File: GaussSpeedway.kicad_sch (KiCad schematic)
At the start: 47 parts

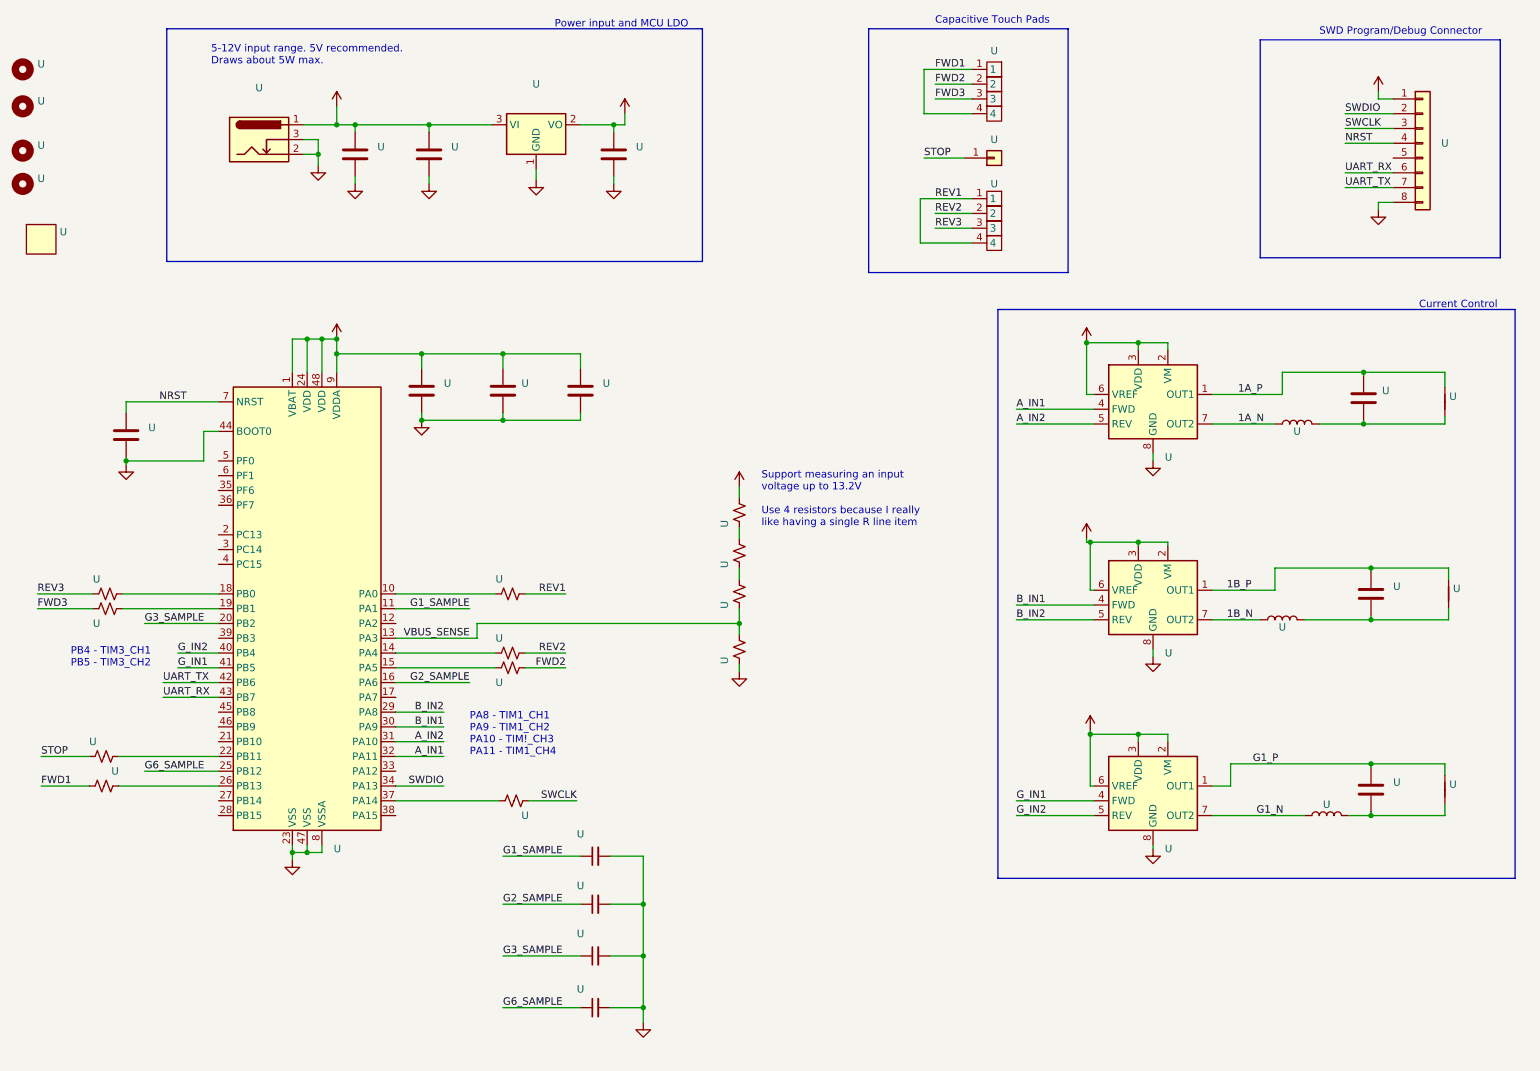
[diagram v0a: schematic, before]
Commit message: Revert an accidental eeschema nightly infection
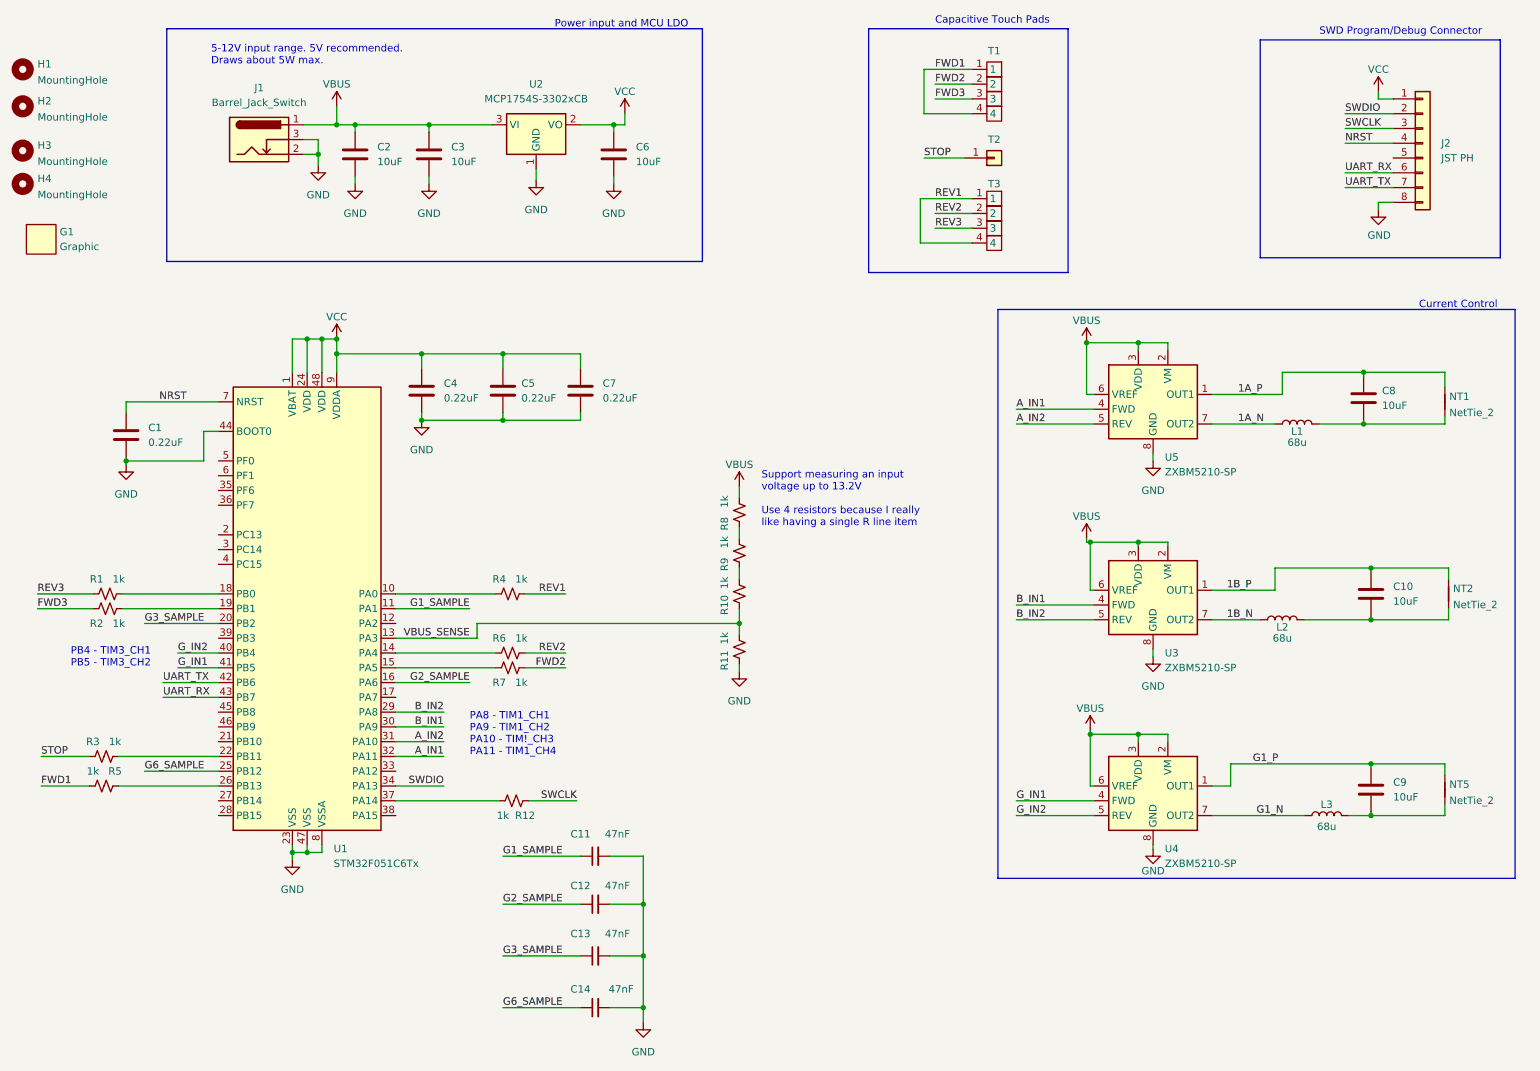
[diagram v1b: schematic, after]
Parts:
- C1, C4, C5, C7: renamed from U; value (none) -> 0.22uF; footprint (none) -> Capacitor_SMD:C_0603_1608Metric
- C10, C2, C3, C6, C8, C9: renamed from U; value (none) -> 10uF; footprint (none) -> Capacitor_SMD:C_0805_2012Metric
- C11, C12, C13, C14: renamed from U; value (none) -> 47nF; footprint (none) -> Capacitor_SMD:C_0603_1608Metric
- G1: renamed from U; value (none) -> Graphic; footprint (none) -> track:magnetlogo
- H1, H2, H3, H4: renamed from U; value (none) -> MountingHole; footprint (none) -> MountingHole:MountingHole_3.5mm
- J1: renamed from U; value (none) -> Barrel_Jack_Switch; footprint (none) -> jmlib:RASM722BK_Barrel
- J2: renamed from U; value (none) -> JST PH; footprint (none) -> Connector_JST:JST_PH_S8B-PH-SM4-TB_1x08-1MP_P2.00mm_Horizontal
- L1, L2, L3: renamed from U; value (none) -> 68u; footprint (none) -> Inductor_SMD:L_Bourns_SRR1260
- NT1, NT2, NT5: renamed from U; value (none) -> NetTie_2; footprint (none) -> NetTie:NetTie-2_SMD_Pad0.5mm
- R1, R10, R11, R12, R2, R3, R4, R5, R6, R7, R8, R9: renamed from U; value (none) -> 1k; footprint (none) -> Resistor_SMD:R_0603_1608Metric
- T1, T3: renamed from U; value (none) -> LinearTouch4; footprint (none) -> touch:linear_touch_40.0mm
- T2: renamed from U; value (none) -> Conn_01x01; footprint (none) -> touch:button
- U1: renamed from U; value (none) -> STM32F051C6Tx; footprint (none) -> Package_QFP:LQFP-48_7x7mm_P0.5mm
- U2: renamed from U; value (none) -> MCP1754S-3302xCB; footprint (none) -> Package_TO_SOT_SMD:SOT-23
- U3, U4, U5: renamed from U; value (none) -> ZXBM5210-SP; footprint (none) -> Package_SO:Diodes_SO-8EP

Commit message: Rename project files
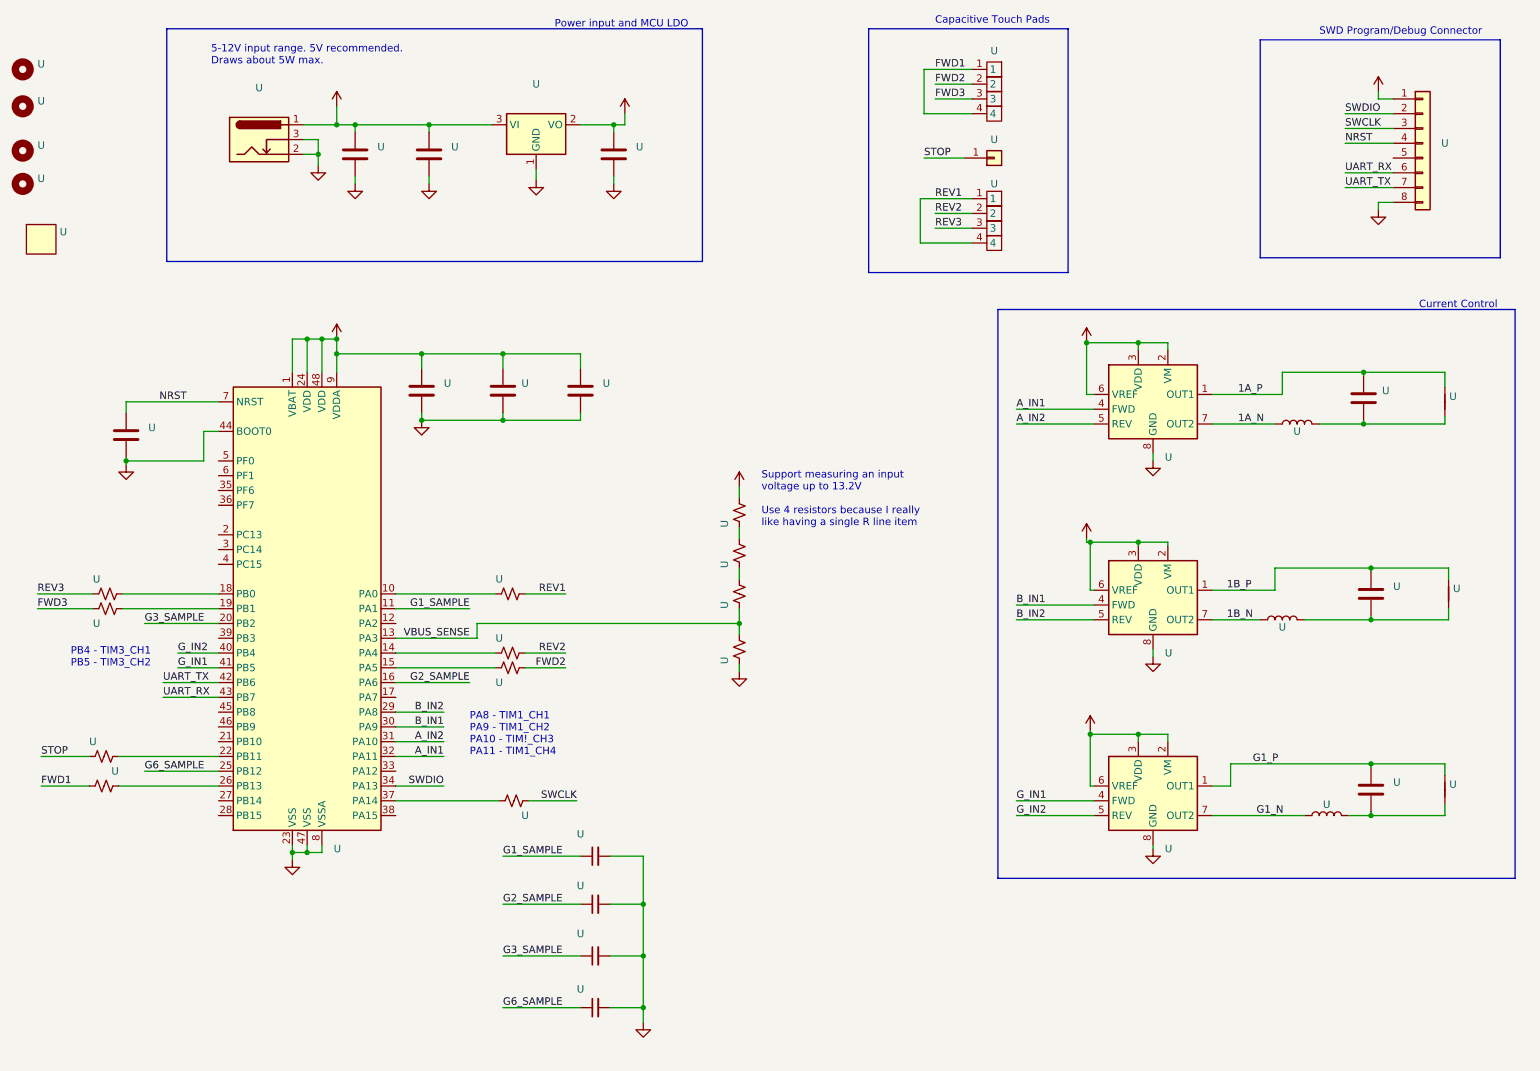
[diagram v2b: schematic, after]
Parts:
- U: renamed from C11; value 47nF -> (none); footprint Capacitor_SMD:C_0603_1608Metric -> (none)
- U: renamed from C3; value 10uF -> (none); footprint Capacitor_SMD:C_0805_2012Metric -> (none)
- U: renamed from C5; value 0.22uF -> (none); footprint Capacitor_SMD:C_0603_1608Metric -> (none)
- U: renamed from T1; value LinearTouch4 -> (none); footprint touch:linear_touch_40.0mm -> (none)
- U: renamed from R12; value 1k -> (none); footprint Resistor_SMD:R_0603_1608Metric -> (none)
- U: renamed from J1; value Barrel_Jack_Switch -> (none); footprint jmlib:RASM722BK_Barrel -> (none)
- U: renamed from R10; value 1k -> (none); footprint Resistor_SMD:R_0603_1608Metric -> (none)
- U: renamed from NT2; value NetTie_2 -> (none); footprint NetTie:NetTie-2_SMD_Pad0.5mm -> (none)
- U: renamed from R9; value 1k -> (none); footprint Resistor_SMD:R_0603_1608Metric -> (none)
- U: renamed from C13; value 47nF -> (none); footprint Capacitor_SMD:C_0603_1608Metric -> (none)
- U: renamed from U4; value ZXBM5210-SP -> (none); footprint Package_SO:Diodes_SO-8EP -> (none)
- U: renamed from C7; value 0.22uF -> (none); footprint Capacitor_SMD:C_0603_1608Metric -> (none)
- U: renamed from R6; value 1k -> (none); footprint Resistor_SMD:R_0603_1608Metric -> (none)
- U: renamed from NT1; value NetTie_2 -> (none); footprint NetTie:NetTie-2_SMD_Pad0.5mm -> (none)
- U: renamed from U2; value MCP1754S-3302xCB -> (none); footprint Package_TO_SOT_SMD:SOT-23 -> (none)
- U: renamed from R3; value 1k -> (none); footprint Resistor_SMD:R_0603_1608Metric -> (none)
- U: renamed from C12; value 47nF -> (none); footprint Capacitor_SMD:C_0603_1608Metric -> (none)
- U: renamed from R4; value 1k -> (none); footprint Resistor_SMD:R_0603_1608Metric -> (none)
- U: renamed from C1; value 0.22uF -> (none); footprint Capacitor_SMD:C_0603_1608Metric -> (none)
- U: renamed from H4; value MountingHole -> (none); footprint MountingHole:MountingHole_3.5mm -> (none)
- U: renamed from C8; value 10uF -> (none); footprint Capacitor_SMD:C_0805_2012Metric -> (none)
- U: renamed from T3; value LinearTouch4 -> (none); footprint touch:linear_touch_40.0mm -> (none)
- U: renamed from R5; value 1k -> (none); footprint Resistor_SMD:R_0603_1608Metric -> (none)
- U: renamed from R8; value 1k -> (none); footprint Resistor_SMD:R_0603_1608Metric -> (none)
- U: renamed from C2; value 10uF -> (none); footprint Capacitor_SMD:C_0805_2012Metric -> (none)
- U: renamed from H1; value MountingHole -> (none); footprint MountingHole:MountingHole_3.5mm -> (none)
- U: renamed from U5; value ZXBM5210-SP -> (none); footprint Package_SO:Diodes_SO-8EP -> (none)
- U: renamed from U1; value STM32F051C6Tx -> (none); footprint Package_QFP:LQFP-48_7x7mm_P0.5mm -> (none)
- U: renamed from R11; value 1k -> (none); footprint Resistor_SMD:R_0603_1608Metric -> (none)
- U: renamed from C14; value 47nF -> (none); footprint Capacitor_SMD:C_0603_1608Metric -> (none)
- U: renamed from L3; value 68u -> (none); footprint Inductor_SMD:L_Bourns_SRR1260 -> (none)
- U: renamed from H3; value MountingHole -> (none); footprint MountingHole:MountingHole_3.5mm -> (none)
- U: renamed from C4; value 0.22uF -> (none); footprint Capacitor_SMD:C_0603_1608Metric -> (none)
- U: renamed from C10; value 10uF -> (none); footprint Capacitor_SMD:C_0805_2012Metric -> (none)
- U: renamed from L1; value 68u -> (none); footprint Inductor_SMD:L_Bourns_SRR1260 -> (none)
- U: renamed from R7; value 1k -> (none); footprint Resistor_SMD:R_0603_1608Metric -> (none)
- U: renamed from U3; value ZXBM5210-SP -> (none); footprint Package_SO:Diodes_SO-8EP -> (none)
- U: renamed from R2; value 1k -> (none); footprint Resistor_SMD:R_0603_1608Metric -> (none)
- U: renamed from L2; value 68u -> (none); footprint Inductor_SMD:L_Bourns_SRR1260 -> (none)
- U: renamed from J2; value JST PH -> (none); footprint Connector_JST:JST_PH_S8B-PH-SM4-TB_1x08-1MP_P2.00mm_Horizontal -> (none)
- U: renamed from C9; value 10uF -> (none); footprint Capacitor_SMD:C_0805_2012Metric -> (none)
- U: renamed from G1; value Graphic -> (none); footprint track:magnetlogo -> (none)
- U: renamed from H2; value MountingHole -> (none); footprint MountingHole:MountingHole_3.5mm -> (none)
- U: renamed from C6; value 10uF -> (none); footprint Capacitor_SMD:C_0805_2012Metric -> (none)
- U: renamed from T2; value Conn_01x01 -> (none); footprint touch:button -> (none)
- U: renamed from R1; value 1k -> (none); footprint Resistor_SMD:R_0603_1608Metric -> (none)
- U: renamed from NT5; value NetTie_2 -> (none); footprint NetTie:NetTie-2_SMD_Pad0.5mm -> (none)
